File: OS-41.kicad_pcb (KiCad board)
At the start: 4 copper layers, 45.2 x 55.8 mm, 80 parts, among them J1 Conn_01x02_Pin, J2 Conn_01x02_Pin, J3 Conn_01x02_Pin, J4 Conn_Coaxial, J5 Conn_01x02_Pin, J6 USB_B_Micro, J7 Conn_01x09_Pin, SW1 TS-1187A-B-A-B, SW2 TS-1187A-B-A-B, U1 GPS1003, U10 W25Q128JVS, U2 SI4432-B1-FMR, U3 MCP1640x-xCHY, U4 ATGM336H-5N31, U5 DS18B20, U6 BMP390L, U7 RP2040, U9 AMS1117-3.3, X1 SMD-3225_4P 30.000MHZ 10PF, X2 ABM8-272-T3_C20625731

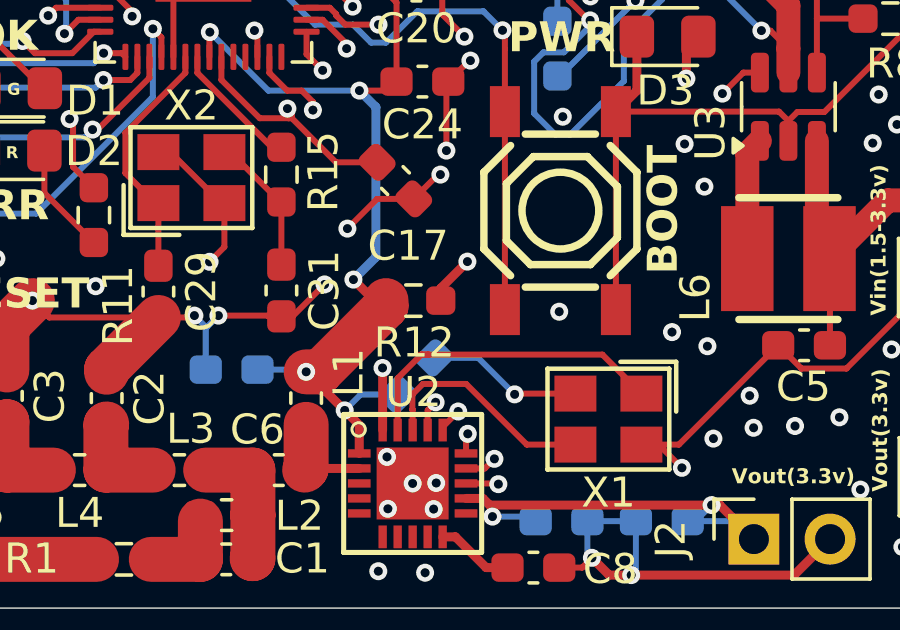
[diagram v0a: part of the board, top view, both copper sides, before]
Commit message: Move a few decoupling capacitors away for the radio IC
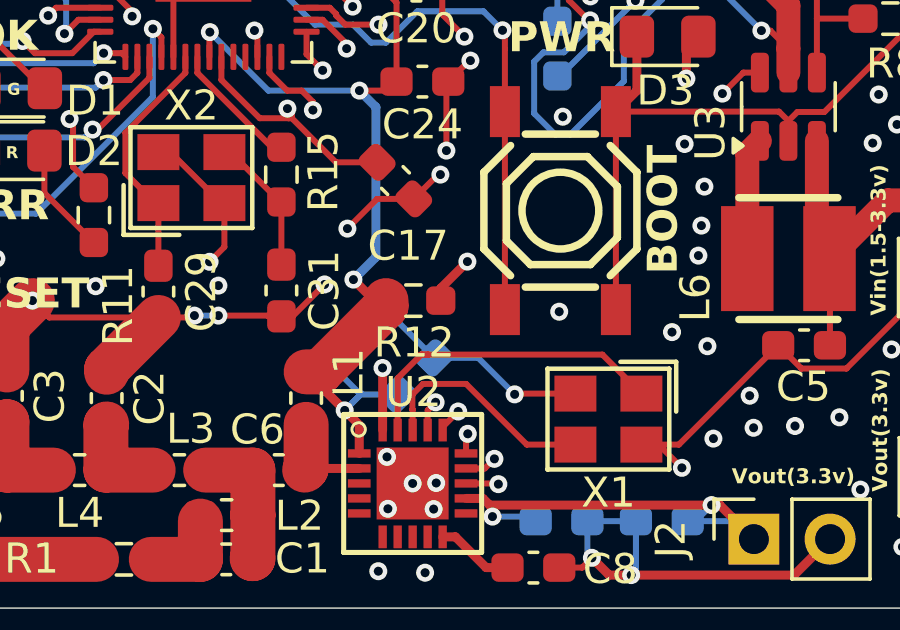
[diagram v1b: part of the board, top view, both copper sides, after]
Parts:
- moved C4 4.58 mm to (116.8, 119.1), turned to 45 degrees
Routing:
- net VCC: track 240.1 -> 241.1 mm, vias 18 -> 17
- net GND: track 341.8 -> 341.7 mm, vias 166 -> 169
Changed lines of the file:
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@@
 	(footprint "Capacitor_SMD:C_0603_1608Metric_Pad1.08x0.95mm_HandSolder"
 		(layer "B.Cu")
-		(at 112.44 120.5 180)
+		(at 116.8 119.1 45)
 		(descr "Capacitor SMD 0603 (1608 Metric), square (rectangular) end terminal, IPC_7351 nominal with elongated pad for handsoldering. (Body size source: IPC-SM-782 page 76, https://www.pcb-3d.com/wordpress/wp-content/uploads/ipc-sm-782a_amendment_1_and_2.pdf), generated with kicad-footprint-generator")
 		(tags "capacitor handsolder")
 		(property "Reference" "C4"
-			(at 0 1.43 0)
+			(at 0.013972 -1.272792 45)
 			(layer "B.SilkS")
 			(effects
@@
 		)
 		(property "Value" "10uF"
-			(at 0 -1.43 0)
+			(at 0 -1.43 45)
 			(layer "B.Fab")
 			(effects
@@
 		)
 		(property "Footprint" "Capacitor_SMD:C_0603_1608Metric_Pad1.08x0.95mm_HandSolder"
-			(at 0 0 0)
+			(at 0 0 -135)
 			(unlocked yes)
 			(layer "B.Fab")
@@
 		)
 		(property "Datasheet" ""
-			(at 0 0 0)
+			(at 0 0 -135)
 			(unlocked yes)
 			(layer "B.Fab")
@@
 		)
 		(property "Description" "Unpolarized capacitor"
-			(at 0 0 0)
+			(at 0 0 -135)
 			(unlocked yes)
 			(layer "B.Fab")
@@
 		(attr smd)
 		(fp_line
-			(start 0.146267 0.51)
-			(end -0.146267 0.51)
+			(start 0.146267 -0.51)
+			(end -0.146267 -0.51)
 			(stroke
 				(width 0.12)
@@
 		)
 		(fp_line
-			(start 0.146267 -0.51)
-			(end -0.146267 -0.51)
+			(start 0.146267 0.51)
+			(end -0.146267 0.51)
 			(stroke
 				(width 0.12)
@@
 		)
 		(fp_line
-			(start 1.65 0.73)
-			(end -1.65 0.73)
+			(start -1.65 -0.73)
+			(end 1.65 -0.73)
 			(stroke
 				(width 0.05)
@@
 		)
 		(fp_line
-			(start 1.65 -0.73)
-			(end 1.65 0.73)
+			(start -1.65 0.73)
+			(end -1.65 -0.73)
 			(stroke
 				(width 0.05)
@@
 		)
 		(fp_line
-			(start -1.65 0.73)
-			(end -1.65 -0.73)
+			(start 1.65 -0.73)
+			(end 1.65 0.73)
 			(stroke
 				(width 0.05)
@@
 		)
 		(fp_line
-			(start -1.65 -0.73)
-			(end 1.65 -0.73)
+			(start 1.65 0.73)
+			(end -1.65 0.73)
 			(stroke
 				(width 0.05)
@@
 		)
 		(fp_line
-			(start 0.8 0.4)
-			(end -0.8 0.4)
+			(start -0.8 -0.4)
+			(end 0.8 -0.4)
 			(stroke
 				(width 0.1)
@@
 		)
 		(fp_line
-			(start 0.8 -0.4)
-			(end 0.8 0.4)
+			(start -0.8 0.4)
+			(end -0.8 -0.4)
 			(stroke
 				(width 0.1)
@@
 		)
 		(fp_line
-			(start -0.8 0.4)
-			(end -0.8 -0.4)
+			(start 0.8 -0.4)
+			(end 0.8 0.4)
 			(stroke
 				(width 0.1)
@@
 		)
 		(fp_line
-			(start -0.8 -0.4)
-			(end 0.8 -0.4)
+			(start 0.8 0.4)
+			(end -0.8 0.4)
 			(stroke
 				(width 0.1)
@@
 		)
 		(fp_text user "${REFERENCE}"
-			(at 0 0 0)
+			(at 0 0 45)
 			(layer "B.Fab")
 			(effects
@@
 		)
 		(pad "1" smd roundrect
-			(at -0.8625 0 180)
+			(at -0.862501 0 45)
 			(size 1.075 0.95)
 			(layers "B.Cu" "B.Paste" "B.Mask")
@@
 		)
 		(pad "2" smd roundrect
-			(at 0.8625 0 180)
+			(at 0.862501 0 45)
 			(size 1.075 0.95)
 			(layers "B.Cu" "B.Paste" "B.Mask")
@@
 	)
 	(via
+		(at 128 116.7)
+		(size 0.6)
+		(drill 0.3)
+		(layers "F.Cu" "B.Cu")
+		(free yes)
+		(net 1)
+	)
+	(via
 		(at 119.24 98.28)
 		(size 0.6)
@@
 	)
 	(via
+		(at 112 117.7)
+		(size 0.6)
+		(drill 0.3)
+		(layers "F.Cu" "B.Cu")
+		(net 1)
+	)
+	(via
 		(at 132.5 93)
 		(size 0.6)
@@
 		(net 1)
 	)
+	(via
+		(at 128.1 115.7)
+		(size 0.6)
+		(drill 0.3)
+		(layers "F.Cu" "B.Cu")
+		(free yes)
+		(net 1)
+	)
 	(segment
 		(start 116.019998 90.12)
@@
 	)
 	(segment
-		(start 112 118.7)
-		(end 111.2 118.7)
-		(width 0.2)
-		(layer "In1.Cu")
-		(net 1)
-	)
-	(segment
 		(start 103.4 88.4)
 		(end 103.8 88.4)
@@
 	(segment
 		(start 112 118.7)
-		(end 112 117.201346)
+		(end 112 117.7)
 		(width 0.2)
 		(layer "In1.Cu")
@@
 	)
 	(segment
+		(start 112 117.7)
+		(end 112 117.201346)
+		(width 0.2)
+		(layer "In1.Cu")
+		(net 1)
+	)
+	(segment
 		(start 120.2 110)
 		(end 120.4 110.2)
@@
 	)
 	(segment
+		(start 119.19 120.11)
+		(end 117.57012 118.49012)
+		(width 0.2)
+		(layer "B.Cu")
+		(net 1)
+	)
+	(segment
 		(start 120.66 120.11)
 		(end 121.875 121.325)
@@
 	)
 	(segment
-		(start 111.5775 120.5)
-		(end 111.5775 119.0775)
-		(width 0.2)
-		(layer "B.Cu")
-		(net 1)
-	)
-	(segment
 		(start 125.9175 127.1925)
 		(end 125.76 127.35)
@@
 	)
 	(segment
-		(start 115.3 104.6)
-		(end 118.6 104.6)
+		(start 111.2 118.7)
+		(end 112 118.7)
 		(width 0.2)
 		(layer "B.Cu")
@@
 	)
 	(segment
-		(start 111.6225 119.0775)
-		(end 112 118.7)
+		(start 115.3 104.6)
+		(end 118.6 104.6)
 		(width 0.2)
 		(layer "B.Cu")
@@
 	)
 	(segment
-		(start 111.5775 119.0775)
-		(end 111.6225 119.0775)
-		(width 0.2)
-		(layer "B.Cu")
-		(net 1)
-	)
-	(segment
 		(start 119.67988 101.37012)
 		(end 119.67988 100.87988)
@@
 	)
 	(segment
-		(start 117.71988 101.02012)
-		(end 119.32988 101.02012)
+		(start 117.57012 118.49012)
+		(end 117.40988 118.49012)
 		(width 0.2)
 		(layer "B.Cu")
@@
 	)
 	(segment
-		(start 111.5775 119.0775)
-		(end 111.2 118.7)
+		(start 117.71988 101.02012)
+		(end 119.32988 101.02012)
 		(width 0.2)
 		(layer "B.Cu")
@@
 	)
 	(via
-		(at 114.925 120.575002)
-		(size 0.6)
-		(drill 0.3)
-		(layers "F.Cu" "B.Cu")
-		(net 2)
-	)
-	(via
 		(at 99.4 103.2)
 		(size 0.6)
@@
 	)
 	(segment
+		(start 116.78024 121.28976)
+		(end 116.209999 121.860001)
+		(width 0.2)
+		(layer "B.Cu")
+		(net 2)
+	)
+	(segment
 		(start 120.725 101.54476)
 		(end 121.18512 102.00488)
@@
 	)
 	(segment
-		(start 114.849998 120.5)
-		(end 114.925 120.575002)
-		(width 0.2)
-		(layer "B.Cu")
-		(net 2)
-	)
-	(segment
 		(start 118.46012 102.58988)
 		(end 120.60012 102.58988)
@@
 	)
 	(segment
-		(start 113.3025 120.5)
-		(end 114.849998 120.5)
-		(width 0.2)
-		(layer "B.Cu")
-		(net 2)
-	)
-	(segment
 		(start 116.74024 121.32976)
 		(end 116.209999 121.860001)
@@
 	)
 	(segment
+		(start 116.19012 119.70988)
+		(end 116.19012 120.77964)
+		(width 0.2)
+		(layer "B.Cu")
+		(net 2)
+	)
+	(segment
 		(start 127.6425 125.55)
 		(end 127.90637 125.55)
@@
 		(width 0.2)
 		(layer "B.Cu")
+		(net 2)
+	)
+	(segment
+		(start 116.19012 120.77964)
+		(end 116.74024 121.32976)
+		(width 0.2)
+		(layer "B.Cu")

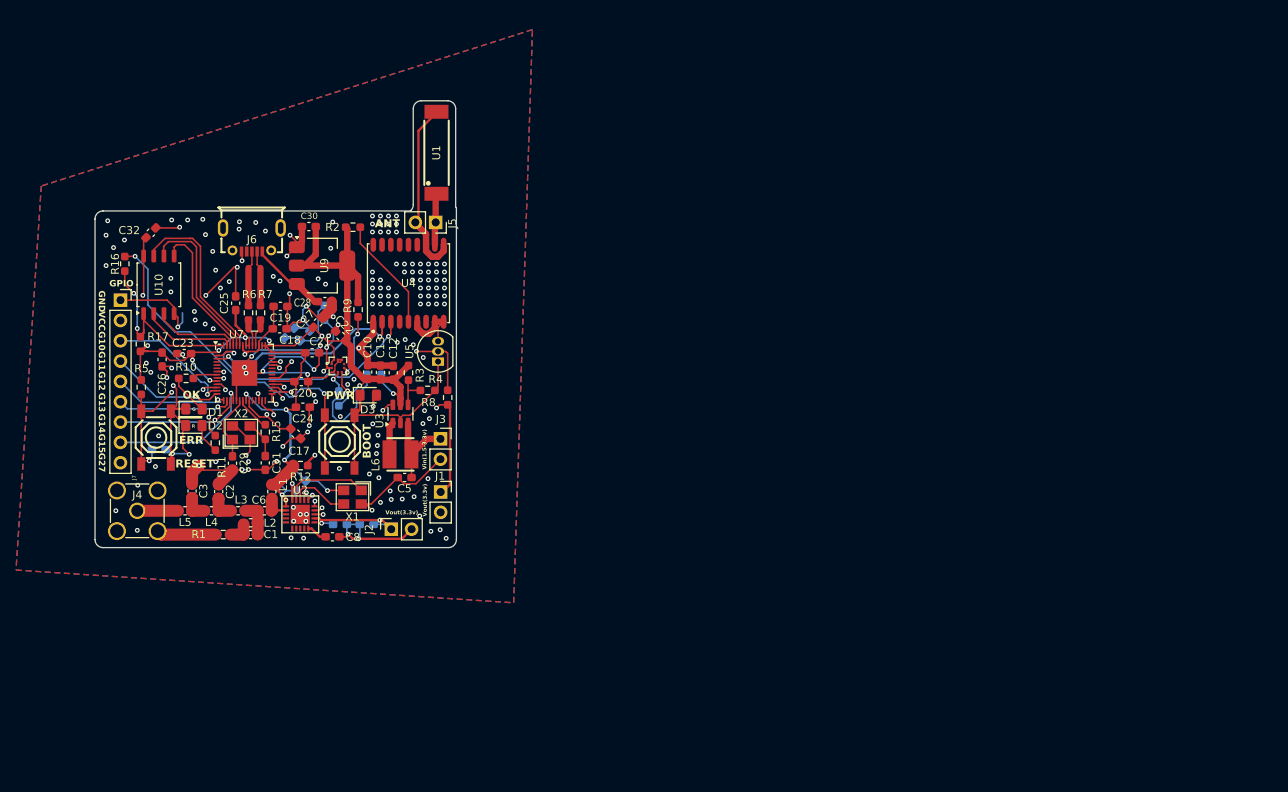
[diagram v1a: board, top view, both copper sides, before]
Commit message: Final RP2040 version (byeeeeeeee RP2040)
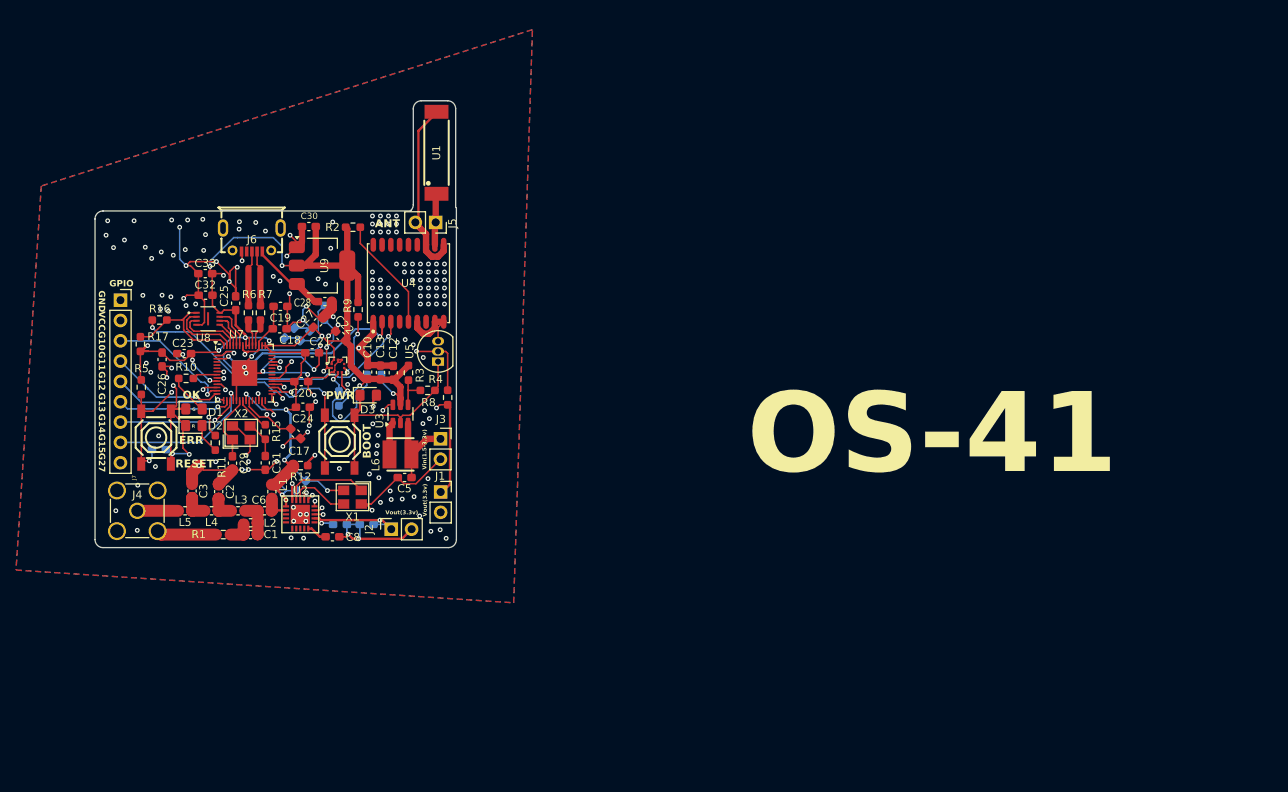
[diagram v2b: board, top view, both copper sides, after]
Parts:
- removed G***: LOGO, LOGO
- removed U10: W25Q128JVS, Package_SO:SOIC-8_5.23x5.23mm_P1.27mm
- added C33: 2.2uF, Capacitor_SMD:C_0603_1608Metric_Pad1.08x0.95mm_HandSolder, F.Cu at (106.6, 94.2)
- added U8: W25Q16JVUXIQ, flash:USON-8_UX_2x3x0p6_WIN, F.Cu at (107.0, 99.8)
- moved C32 10.4 mm to (106.6, 96.9), turned to 180 degrees
- moved R16 8.26 mm to (100.9, 100.0), turned to 0 degrees
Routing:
- net VCC: track 241.1 -> 272.5 mm, vias 17 -> 20
- net QSPI_SD3: track 22.2 -> 5.34 mm
- net QSPI_SCLK: track 20.3 -> 4.50 mm
- net QSPI_SD0: track 17.6 -> 3.40 mm
- net GND: track 341.7 -> 352.6 mm, vias 169 -> 174
- net QSPI_SS: track 26.0 -> 15.8 mm, vias 2 -> 0
- net USB_BOOT: track 44.9 -> 36.1 mm
- net QSPI_SD1: track 11.6 -> 8.65 mm
- net QSPI_SD2: track 10.8 -> 8.00 mm
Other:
- board text added: "OS-41"

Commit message: Remove PCB board, start work on STM32F411
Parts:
- removed C1: 12pF, Capacitor_SMD:C_0603_1608Metric_Pad1.08x0.95mm_HandSolder
- removed C10: 22uF, Capacitor_SMD:C_0603_1608Metric_Pad1.08x0.95mm_HandSolder
- removed C11, C28, C30, C4: 10uF, Capacitor_SMD:C_0603_1608Metric_Pad1.08x0.95mm_HandSolder
- removed C12, C14, C15, C16, C17, C19, C20, C22, C23, C24, C25, C26, C27, C32, C7, C9: 100nF, Capacitor_SMD:C_0603_1608Metric_Pad1.08x0.95mm_HandSolder
- removed C13, C18, C21, C8: 1uF, Capacitor_SMD:C_0603_1608Metric_Pad1.08x0.95mm_HandSolder
- removed C2: 8.2pF, Capacitor_SMD:C_0603_1608Metric_Pad1.08x0.95mm_HandSolder
- removed C29, C31: 15pF, Capacitor_SMD:C_0603_1608Metric_Pad1.08x0.95mm_HandSolder
- removed C3: 9.1pF, Capacitor_SMD:C_0603_1608Metric_Pad1.08x0.95mm_HandSolder
- removed C33: 2.2uF, Capacitor_SMD:C_0603_1608Metric_Pad1.08x0.95mm_HandSolder
- removed C5: 4.7uF, Capacitor_SMD:C_0603_1608Metric_Pad1.08x0.95mm_HandSolder
- removed C6: 120pF, Capacitor_SMD:C_0603_1608Metric_Pad1.08x0.95mm_HandSolder
- removed D1, D2, D3: LED, LED_SMD:LED_0805_2012Metric_Pad1.15x1.40mm_HandSolder
- removed J1, J2, J3, J5: Conn_01x02_Pin, Connector_PinSocket_2.54mm:PinSocket_1x02_P2.54mm_Vertical
- removed J4: Conn_Coaxial, Connector_Coaxial:SMA_Amphenol_901-144_Vertical
- removed J6: USB_B_Micro, libsos41:MICRO-USB-SMD_MICRO-USB-18
- removed J7: Conn_01x09_Pin, Connector_PinSocket_2.54mm:PinSocket_1x09_P2.54mm_Vertical
- removed L1: 270nH, Inductor_SMD:L_0603_1608Metric_Pad1.05x0.95mm_HandSolder
- removed L2: 11nH, Inductor_SMD:L_0603_1608Metric_Pad1.05x0.95mm_HandSolder
- removed L3, L5: 24nH, Inductor_SMD:L_0603_1608Metric_Pad1.05x0.95mm_HandSolder
- removed L4: 39nH, Inductor_SMD:L_0603_1608Metric_Pad1.05x0.95mm_HandSolder
- removed L6: 4.7uH, libsos41:IND-SMD_L3.3-W3.0
- removed R1: 50, Resistor_SMD:R_0603_1608Metric_Pad0.98x0.95mm_HandSolder
- removed R10, R11, R12, R15, R16: 1k, Resistor_SMD:R_0603_1608Metric_Pad0.98x0.95mm_HandSolder
- removed R13, R14, R18, R2, R5, R9: 10k, Resistor_SMD:R_0603_1608Metric_Pad0.98x0.95mm_HandSolder
- removed R17: DNF, Resistor_SMD:R_0603_1608Metric_Pad0.98x0.95mm_HandSolder
- removed R3: 976k, Resistor_SMD:R_0603_1608Metric_Pad0.98x0.95mm_HandSolder
- removed R4: 562k, Resistor_SMD:R_0603_1608Metric_Pad0.98x0.95mm_HandSolder
- removed R6, R7: 27.4, Resistor_SMD:R_0603_1608Metric_Pad0.98x0.95mm_HandSolder
- removed R8: 4.7k, Resistor_SMD:R_0603_1608Metric_Pad0.98x0.95mm_HandSolder
- removed SW1, SW2: TS-1187A-B-A-B, libsos41:SW-SMD_4P-L5.1-W5.1-P3.70-LS6.5-TL-2
- removed U1: GPS1003, libsos41:ANT-SMD_L10.0-W3.0
- removed U2: SI4432-B1-FMR, libsos41:QLP20
- removed U3: MCP1640x-xCHY, Package_TO_SOT_SMD:SOT-23-6
- removed U4: ATGM336H-5N31, libsos41:GPSM-SMD_ATGM336H-TR
- removed U5: DS18B20, Package_TO_SOT_THT:TO-92_Inline
- removed U6: BMP390L, libsos41:LGA-10_L2.0-W2.0-P0.50-TL_BMP390L
- removed U7: RP2040, Package_DFN_QFN:QFN-56-1EP_7x7mm_P0.4mm_EP3.2x3.2mm
- removed U8: W25Q16JVUXIQ, flash:USON-8_UX_2x3x0p6_WIN
- removed U9: AMS1117-3.3, Package_TO_SOT_SMD:SOT-223-3_TabPin2
- removed X1: SMD-3225_4P 30.000MHZ 10PF, libsos41:CRYSTAL-SMD_4P-L3.2-W2.5-BL
- removed X2: ABM8-272-T3_C20625731, libsos41:CRYSTAL-SMD_4P-L3.2-W2.5-BL
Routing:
- net GND: track 352.6 -> 0.00 mm, vias 174 -> 0
- net VCC: track 272.5 -> 0.00 mm, vias 20 -> 0
- net BATT: track 41.7 -> 0.00 mm, vias 2 -> 0
- net USB_BOOT: track 36.1 -> 0.00 mm, vias 2 -> 0
- net RXD: track 30.8 -> 0.00 mm, vias 2 -> 0
- net RESET: track 30.6 -> 0.00 mm, vias 3 -> 0
- net DQ: track 28.5 -> 0.00 mm, vias 2 -> 0
- net GPIO27_ADC1: track 26.4 -> 0.00 mm, vias 1 -> 0
- net 1V1: track 26.1 -> 0.00 mm, vias 2 -> 0
- net TXD: track 24.8 -> 0.00 mm, vias 2 -> 0
- net SDN: track 22.3 -> 0.00 mm, vias 2 -> 0
- net NSEL: track 21.7 -> 0.00 mm, vias 2 -> 0
- net NIRQ: track 20.4 -> 0.00 mm, vias 2 -> 0
- net SDO: track 19.5 -> 0.00 mm, vias 2 -> 0
- net GPIO15: track 18.7 -> 0.00 mm, vias 1 -> 0
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- removed copper zone on B.Cu, net GND
- removed copper zone on F.Cu, net GND
- removed copper zone on In1.Cu, net GND
- removed copper zone on In2.Cu, net GND
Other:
- board outline removed
- board text removed: "+"
- board text removed: "-"
- board text removed: "ANT"
- board text removed: "BOOT"
- board text removed: "ERR"
- board text removed: "Ext. Temp."
- board text removed: "G"
- board text removed: "G10"
- board text removed: "G11"
- board text removed: "G12"
- board text removed: "G13"
- board text removed: "G14"
- board text removed: "G15"
- board text removed: "G27"
- board text removed: "GND"
- board text removed: "GPIO"
- board text removed: "GPS Ant."
- board text removed: "Micro USB Program + Debug"
- board text removed: "OK"
- board text removed: "OS-41"
- board text removed: "PWR"
- board text removed: "R"
- board text removed: "RESET"
- board text removed: "VCC"
- board text removed: "Vin(1.5-3.3v)"
- board text removed: "Vout(3.3v)"
